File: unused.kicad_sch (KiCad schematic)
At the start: 1 part, among them U1 NX1H35 PBGA625

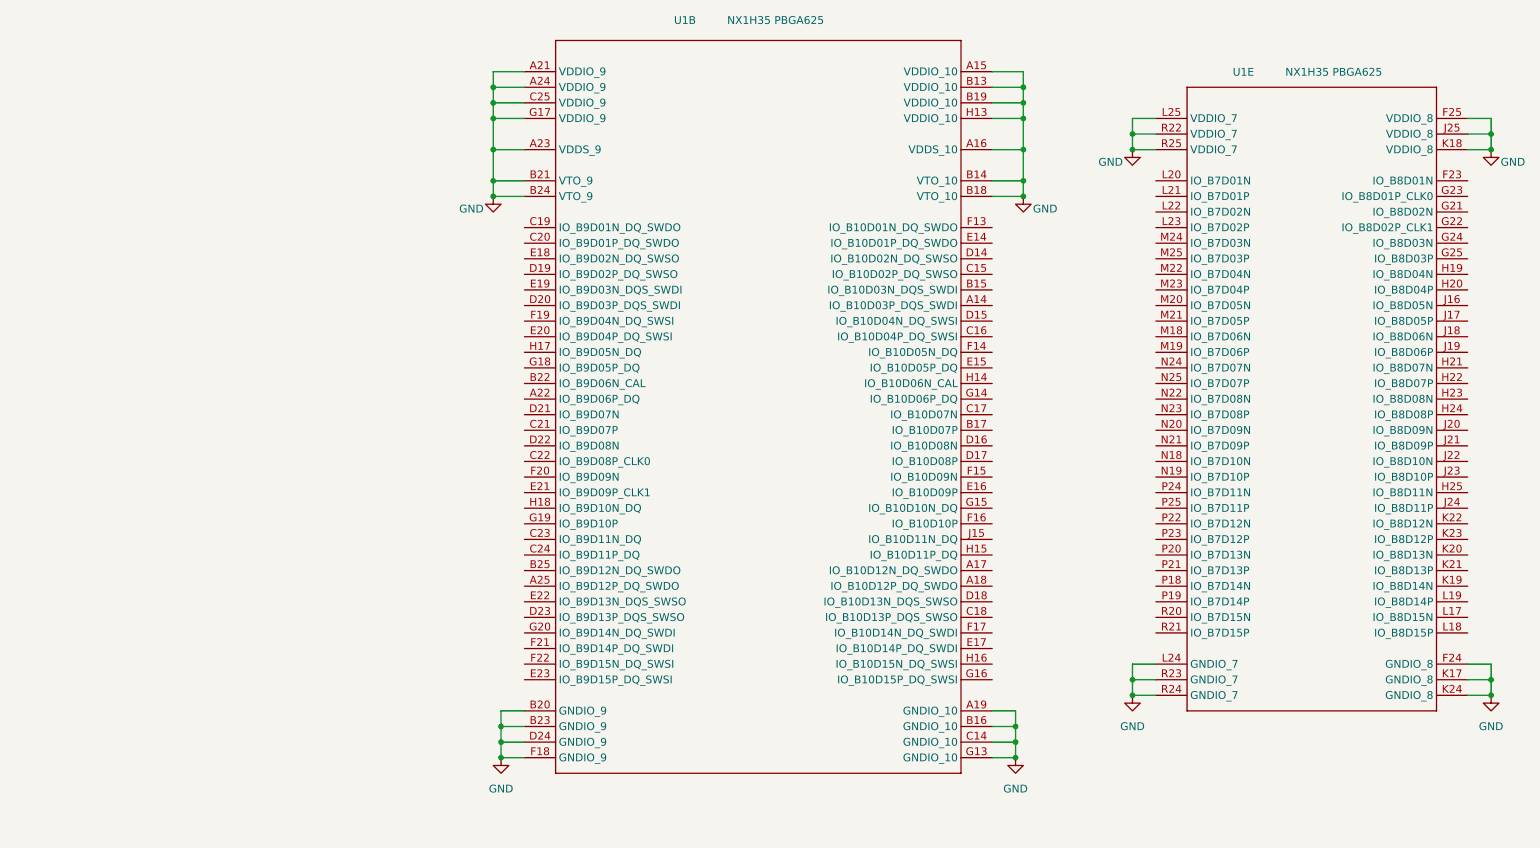
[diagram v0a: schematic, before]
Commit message: SDRAM, bank5
last iteration of sdram. max optimization routing and space wise. Traced 2 frams to Bank 5. Fanout of bank 5 for DF9
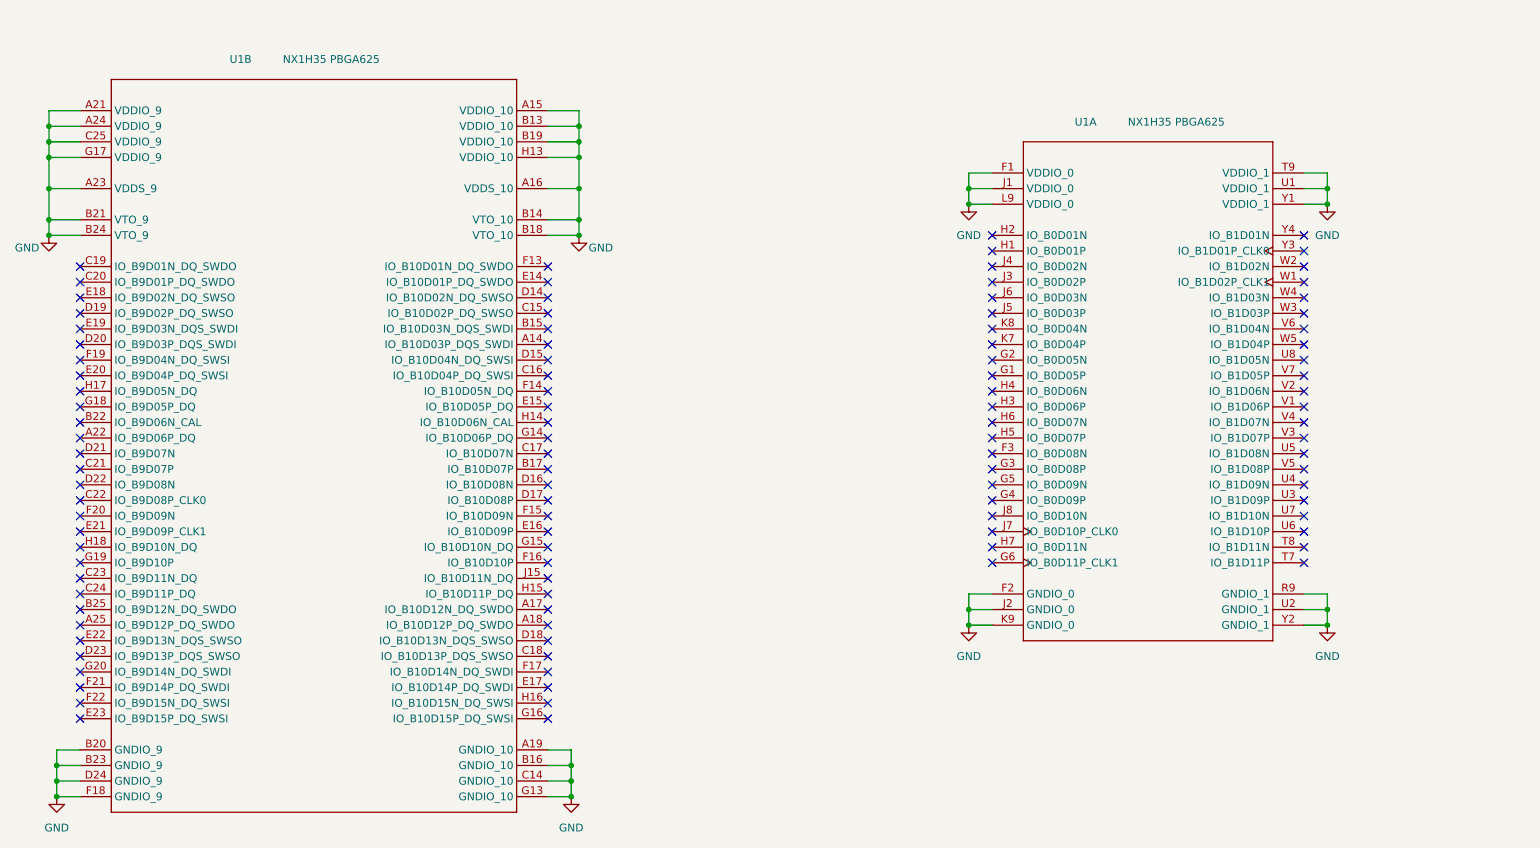
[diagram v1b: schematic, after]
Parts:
- removed unit 5 of U1
- added unit 1 of U1
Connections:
- net GND: now also U1.F1 (VDDIO_0), U1.F2 (GNDIO_0), U1.J1 (VDDIO_0), U1.J2 (GNDIO_0), U1.K9 (GNDIO_0), U1.L9 (VDDIO_0), U1.R9 (GNDIO_1), U1.T9 (VDDIO_1), U1.U1 (VDDIO_1), U1.U2 (GNDIO_1), U1.Y1 (VDDIO_1), U1.Y2 (GNDIO_1)
- no-connect marks 0 -> 104
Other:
- moved on the sheet: U1B

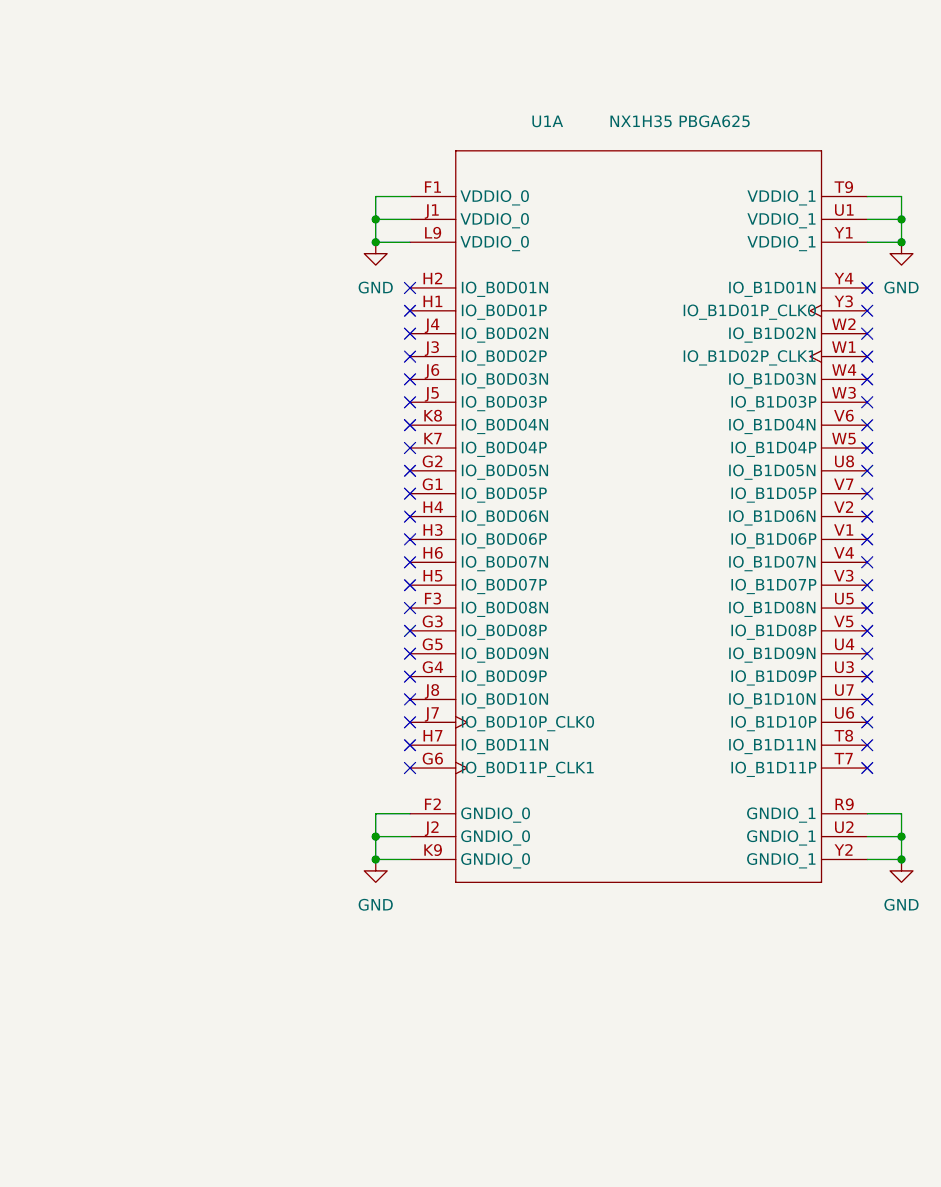
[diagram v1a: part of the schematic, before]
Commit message: full components, LEDS, changed edges
all components on pcb editor. added and  routed leds and 2 PLL. changed edges o have more space
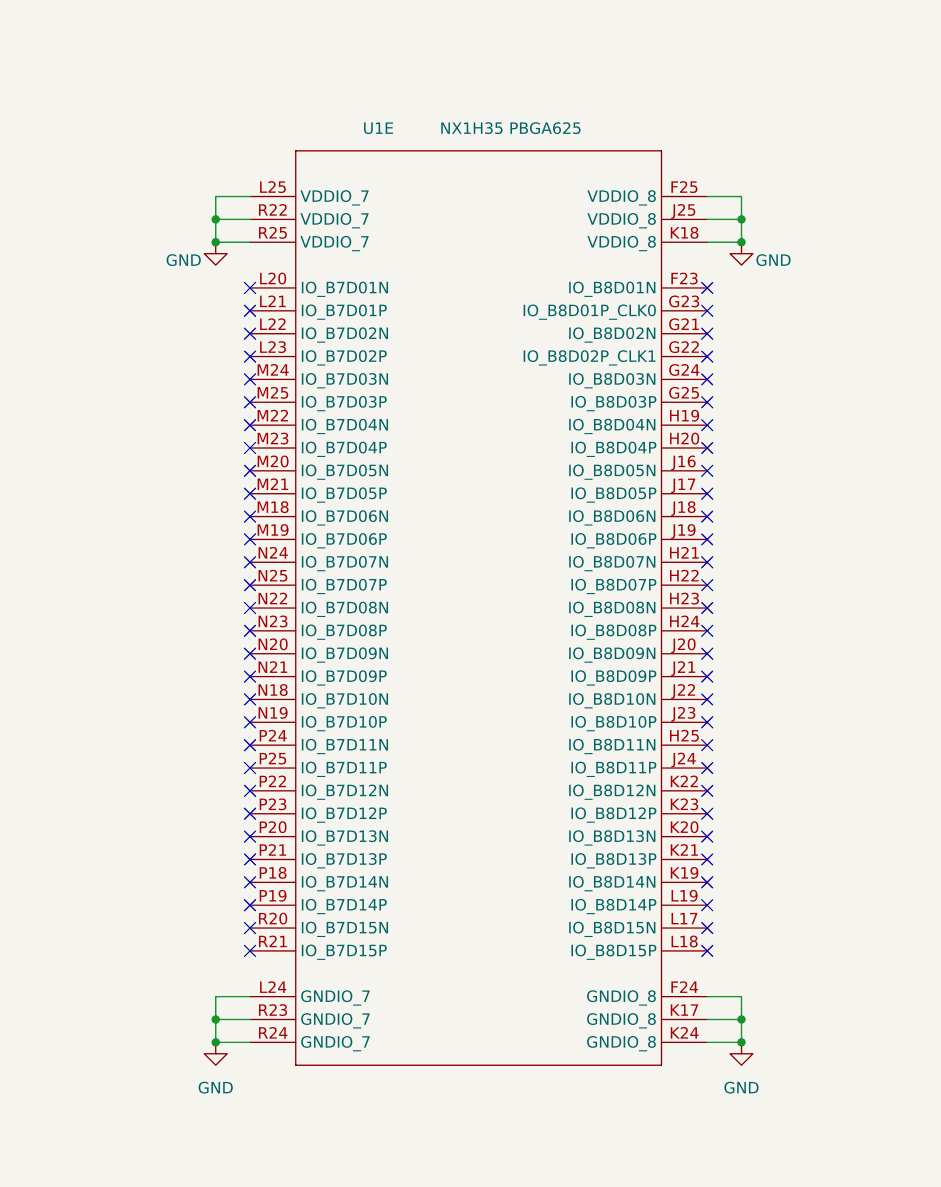
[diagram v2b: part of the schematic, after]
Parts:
- removed unit 1 of U1
- added unit 5 of U1
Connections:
- net GND: now also U1.F24 (GNDIO_8), U1.F25 (VDDIO_8), U1.J25 (VDDIO_8), U1.K17 (GNDIO_8), U1.K18 (VDDIO_8), U1.K24 (GNDIO_8), U1.L24 (GNDIO_7), U1.L25 (VDDIO_7), U1.R22 (VDDIO_7), U1.R23 (GNDIO_7), U1.R24 (GNDIO_7), U1.R25 (VDDIO_7)
- no-connect marks 104 -> 120

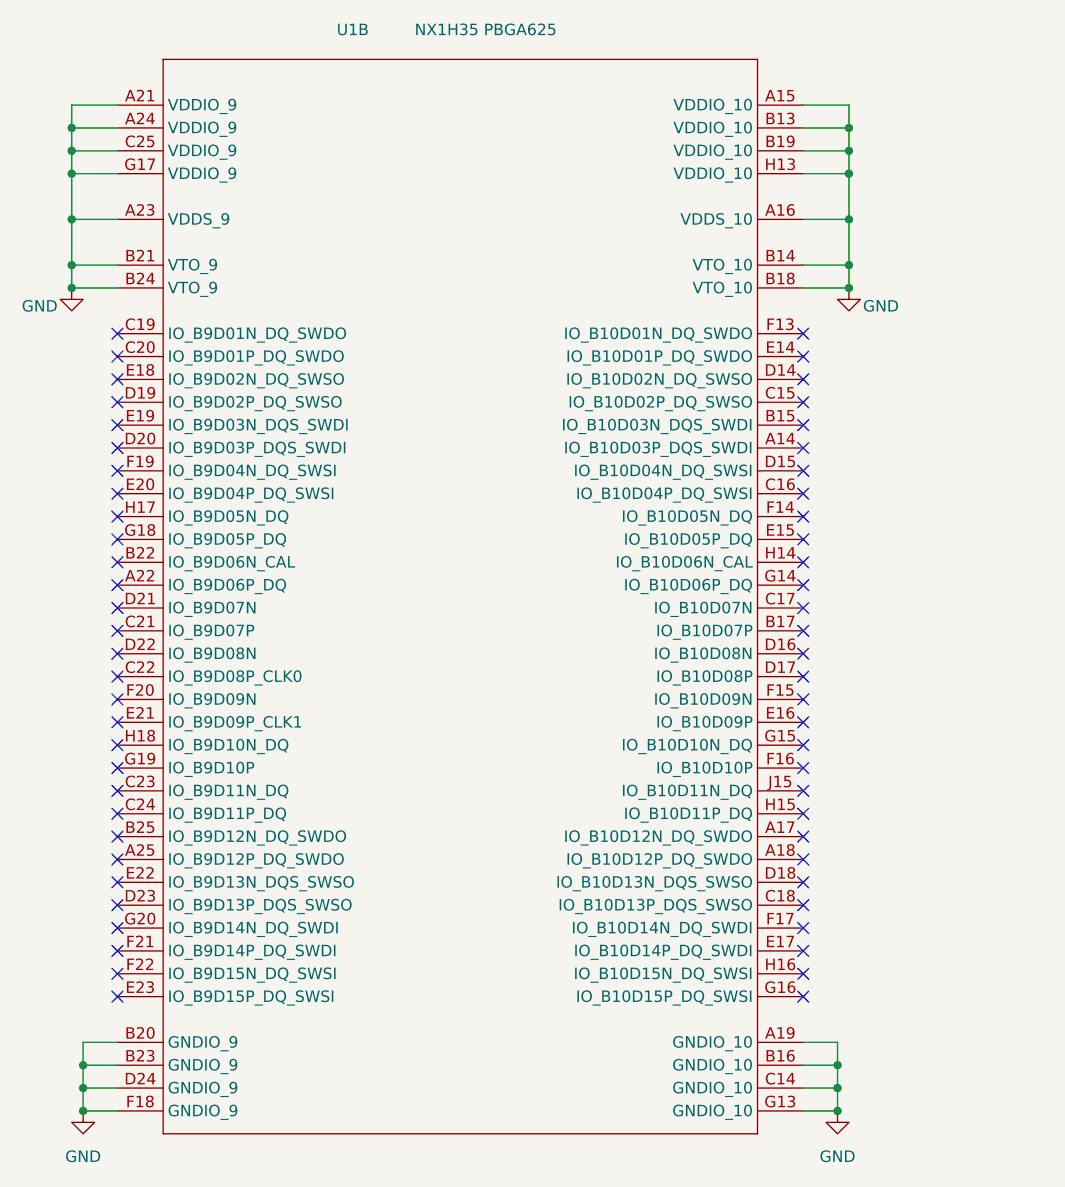
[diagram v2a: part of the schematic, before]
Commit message: SPW Bank0
completed SPW, rotated edges and adjusted dimensions to make the extra sdram bga fit. completed Bank 0 (still to route to connector). Started fanout of bga sdram
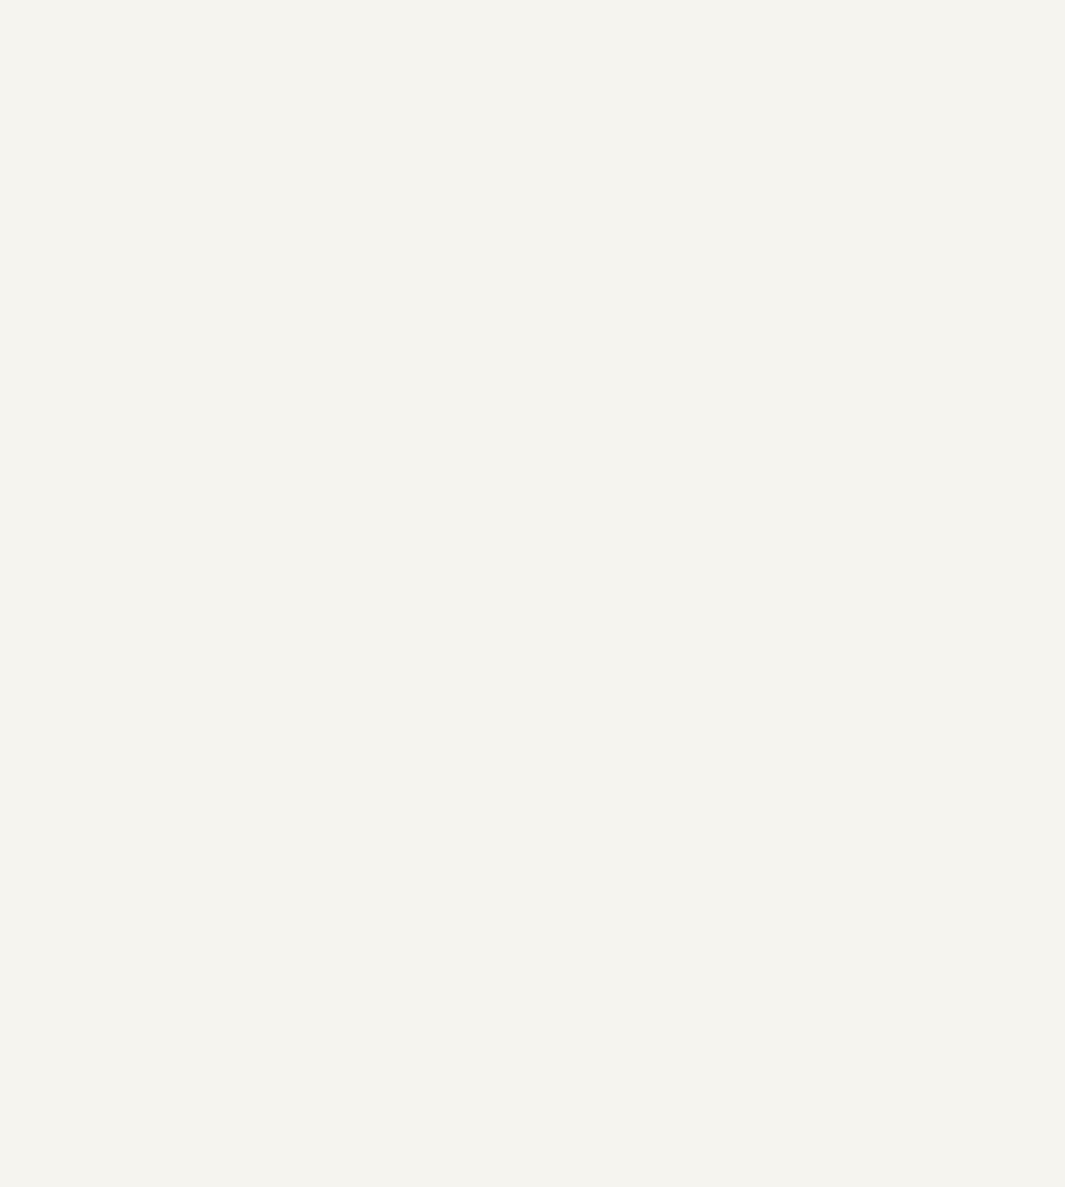
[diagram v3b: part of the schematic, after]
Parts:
- removed unit 2 of U1
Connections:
- no-connect marks 120 -> 60

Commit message: power tree
power tree defined. Few changes remaining but almost finalized
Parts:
- removed U1: NX1H35 PBGA625, DataHub_NG_Medium:NX1H35S_CLGA625, symbol Brave625:root_0_BRAVE625A_Brave625.SchLib
- added C111, C112, C113, C114, C115, C116, C117, C118, C119, C120, C121, C122, C123, C124, C125, C126, C128, C130: 10uF, Capacitor_SMD:C_0603_1608Metric_Pad1.08x0.95mm_HandSolder, symbol Device:C_Small
- added C127, C129: 4.7nF, Capacitor_SMD:C_0603_1608Metric_Pad1.08x0.95mm_HandSolder, symbol Device:C_Small
- added R44, R45, R57: 100k, Resistor_SMD:R_0402_1005Metric_Pad0.72x0.64mm_HandSolder, symbol Device:R_Small
- added R47, R55: 3k74, Resistor_SMD:R_0402_1005Metric_Pad0.72x0.64mm_HandSolder, symbol Device:R_Small
- added R48, R52: 4k02, Resistor_SMD:R_0402_1005Metric_Pad0.72x0.64mm_HandSolder, symbol Device:R_Small
- added R49, R51, R53: 1k, Resistor_SMD:R_0402_1005Metric_Pad0.72x0.64mm_HandSolder, symbol Device:R_Small
- added R50: 1k4, Resistor_SMD:R_0402_1005Metric_Pad0.72x0.64mm_HandSolder, symbol Device:R_Small
- added R54, R56: 1k2, Resistor_SMD:R_0402_1005Metric_Pad0.72x0.64mm_HandSolder, symbol Device:R_Small
- added U12, U13, U14: MAX8556ETE, DataHub_Footprints:MAX8556, symbol MAX_LDO:MAX8556ETE
- added U15, U16: TPS74201RGWR, DataHub_Footprints:TPS74201, symbol TPS_LDO:TPS74201RGWR
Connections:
- net GND: now also C111.2, C112.2, C113.2, C114.2, C115.2, C116.2, C117.2, C118.2, C119.2, C120.2, C121.2, C122.2, C123.2, C124.2, C125.2, C126.2, C127.1, C128.2, C129.1, C130.2, R49.2, R51.2, R53.2, R54.2, R56.2, U12.14 (GND), U12.15 (NC), U12.17 (EPAD), U13.14 (GND), U13.15 (NC), U13.17 (EPAD), U14.14 (GND), U14.15 (NC), U14.17 (EPAD), U15.12 (GND), U15.21 (PAD), U16.12 (GND), U16.21 (PAD)
- new net: R45.2, U13.12 (POK(POR)), U15.11 (EN)
- new net: R52.2, R53.1, U14.13 (FB)
- new net: R55.2, R56.1, U16.16 (FB)
- new net: C129.2, U16.15 (SS)
- new net: R50.2, R51.1, U13.13 (FB)
- new net: R48.2, R49.1, U12.13 (FB)
- new net: R47.2, R54.1, U15.16 (FB)
- new net: C127.2, U15.15 (SS)
- new net: R44.2, U12.12 (POK(POR)), U13.16 (EN)
- new net +1V7_IN: C112.1, C114.1, U13.1 (IN), U13.2 (IN), U13.3 (IN), U13.4 (IN), U13.5 (IN), U13.6 (IN)
- new net +3V3_IN: C111.1, C113.1, C115.1, C116.1, R44.1, R45.1, R57.1, U12.1 (IN), U12.16 (EN), U12.2 (IN), U12.3 (IN), U12.4 (IN), U12.5 (IN), U12.6 (IN), U14.1 (IN), U14.2 (IN), U14.3 (IN), U14.4 (IN), U14.5 (IN), U14.6 (IN)
- new net +3V6_IN: C117.1, C126.1, U15.5 (IN), U15.6 (IN), U15.7 (IN), U15.8 (IN), U16.5 (IN), U16.6 (IN), U16.7 (IN), U16.8 (IN)
- new net +5V_IN: C125.1, C128.1, U15.10 (BIAS), U16.10 (BIAS)
- new net PG_LDO_SERVICE: R57.2, U14.16 (EN), U15.9 (PG), U16.11 (EN)
- new net VDD1V2: C119.1, C121.1, R50.1, U13.10 (OUT), U13.11 (OUT), U13.7 (OUT), U13.8 (OUT), U13.9 (OUT)
- new net VDD2V5: C122.1, C123.1, R52.1, U14.10 (OUT), U14.11 (OUT), U14.7 (OUT), U14.8 (OUT), U14.9 (OUT)
- new net VDD2V5A: C118.1, C120.1, R48.1, U12.10 (OUT), U12.11 (OUT), U12.7 (OUT), U12.8 (OUT), U12.9 (OUT)
- new net VDD3V3: C130.1, R55.1, U16.1 (OUT), U16.18 (OUT), U16.19 (OUT), U16.20 (OUT)
- new net VDDIO_SERVICE: C124.1, R47.1, U15.1 (OUT), U15.18 (OUT), U15.19 (OUT), U15.20 (OUT)
- no-connect marks 60 -> 14
